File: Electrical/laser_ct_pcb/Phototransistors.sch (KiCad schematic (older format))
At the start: 48 parts, among them Q1 Q_Photo_NPN, Q10 Q_Photo_NPN, Q11 Q_Photo_NPN, Q12 Q_Photo_NPN, Q13 Q_Photo_NPN, Q14 Q_Photo_NPN, Q15 Q_Photo_NPN, Q16 Q_Photo_NPN, Q17 Q_Photo_NPN, Q18 Q_Photo_NPN, Q19 Q_Photo_NPN, Q2 Q_Photo_NPN, Q20 Q_Photo_NPN, Q21 Q_Photo_NPN, Q22 Q_Photo_NPN, Q23 Q_Photo_NPN, Q24 Q_Photo_NPN, Q3 Q_Photo_NPN, Q4 Q_Photo_NPN, Q5 Q_Photo_NPN, Q6 Q_Photo_NPN, Q7 Q_Photo_NPN, Q8 Q_Photo_NPN, Q9 Q_Photo_NPN

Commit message: End of Episode 08.
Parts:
- removed Q1, Q2, Q3, Q4: Q_Photo_NPN, LED_THT:LED_D3.0mm, symbol Device:Q_Photo_NPN
- removed Q10, Q11, Q12, Q13, Q14, Q15, Q16, Q17, Q18, Q19, Q20, Q21, Q22, Q23, Q24, Q5, Q6, Q7, Q8, Q9: Q_Photo_NPN, symbol Device:Q_Photo_NPN
- removed R1, R2, R3, R4: 1 kOhm, Resistor_SMD:R_1206_3216Metric, symbol Device:R_US
- removed R10, R11, R12, R13, R14, R15, R16, R17, R18, R19, R20, R21, R22, R23, R24, R5, R6, R7, R8, R9: 1 kOhm, symbol Device:R_US
- added Q? (x24): Q_Photo_NPN, symbol Device:Q_Photo_NPN
- added R? (x24): 1 kOhm, symbol Device:R_US
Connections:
- net +5V: now also R?.1, R?.1, R?.1, R?.1, R?.1, R?.1, R?.1, R?.1, R?.1, R?.1, R?.1, R?.1, R?.1, R?.1, R?.1, R?.1, R?.1, R?.1, R?.1, R?.1, R?.1, R?.1, R?.1, R?.1
- net GND: now also Q?.2 (E), Q?.2 (E), Q?.2 (E), Q?.2 (E), Q?.2 (E), Q?.2 (E), Q?.2 (E), Q?.2 (E), Q?.2 (E), Q?.2 (E), Q?.2 (E), Q?.2 (E), Q?.2 (E), Q?.2 (E), Q?.2 (E), Q?.2 (E), Q?.2 (E), Q?.2 (E), Q?.2 (E), Q?.2 (E), Q?.2 (E), Q?.2 (E), Q?.2 (E), Q?.2 (E)
- new net PT1: Q?.1 (C), R?.2
- new net PT10: Q?.1 (C), R?.2
- new net PT11: Q?.1 (C), R?.2
- new net PT12: Q?.1 (C), R?.2
- new net PT13: Q?.1 (C), R?.2
- new net PT14: Q?.1 (C), R?.2
- new net PT15: Q?.1 (C), R?.2
- new net PT16: Q?.1 (C), R?.2
- new net PT17: Q?.1 (C), R?.2
- new net PT18: Q?.1 (C), R?.2
- new net PT19: Q?.1 (C), R?.2
- new net PT2: Q?.1 (C), R?.2
- new net PT20: Q?.1 (C), R?.2
- new net PT21: Q?.1 (C), R?.2
- new net PT22: Q?.1 (C), R?.2
- new net PT23: Q?.1 (C), R?.2
- new net PT24: Q?.1 (C), R?.2
- new net PT3: Q?.1 (C), R?.2
- new net PT4: Q?.1 (C), R?.2
- new net PT5: Q?.1 (C), R?.2
- new net PT6: Q?.1 (C), R?.2
- new net PT7: Q?.1 (C), R?.2
- new net PT8: Q?.1 (C), R?.2
- new net PT9: Q?.1 (C), R?.2

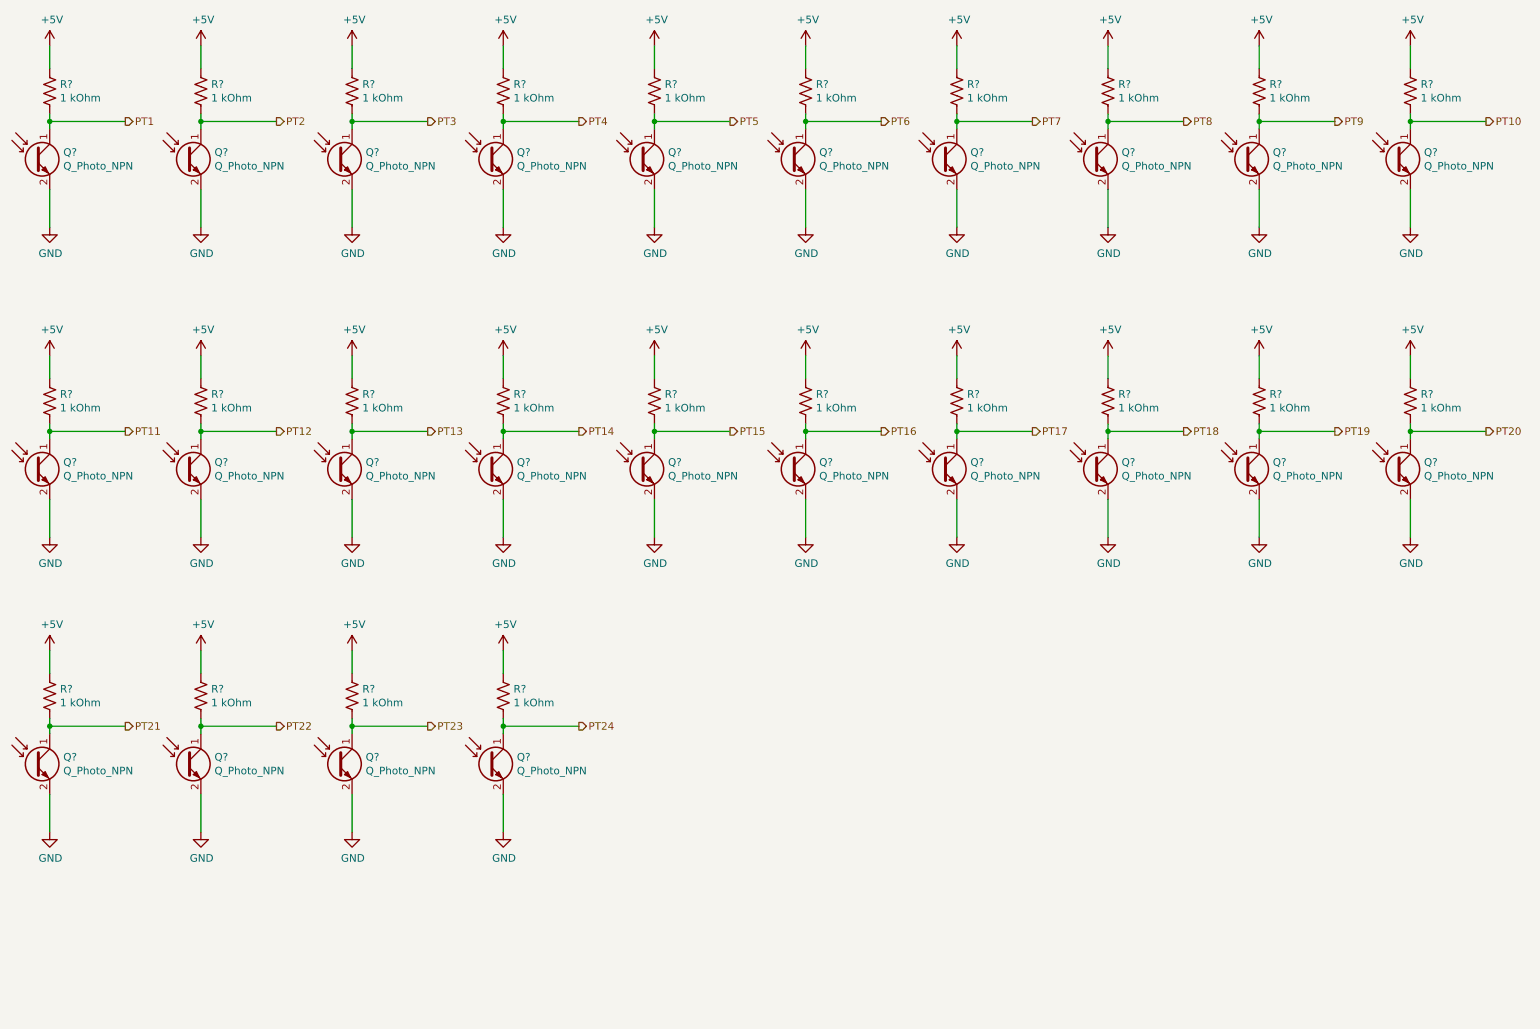
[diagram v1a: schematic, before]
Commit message: Fixed through hole size on ICSP board.
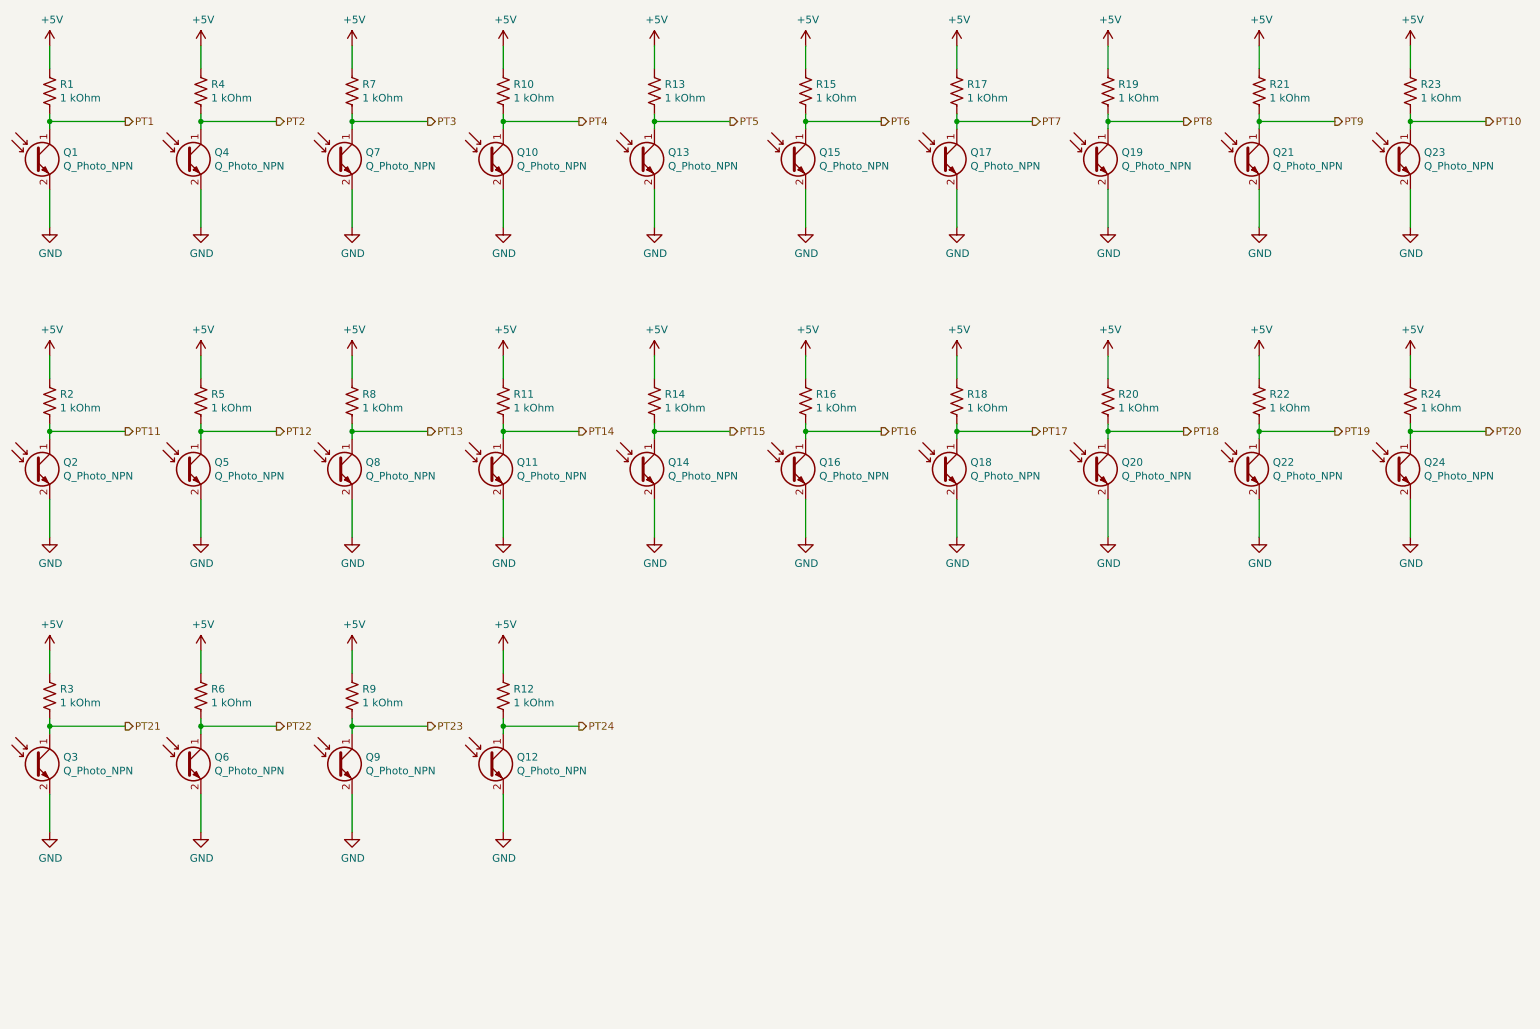
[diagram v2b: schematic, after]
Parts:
- Q1, Q10, Q11, Q12, Q13, Q14, Q15, Q16, Q17, Q18, Q19, Q2, Q20, Q21, Q22, Q23, Q24, Q3, Q4, Q5, Q6, Q7, Q8, Q9: renamed from Q?; footprint (none) -> laser_ct:LTR_301
- R1, R10, R11, R12, R13, R14, R15, R16, R17, R18, R19, R2, R20, R21, R22, R23, R24, R3, R4, R5, R6, R7, R8, R9: renamed from R?; footprint (none) -> Resistor_THT:R_Axial_DIN0204_L3.6mm_D1.6mm_P7.62mm_Horizontal

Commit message: End of episode 09.
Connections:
- net PT10: now also Q10.1 (C), R10.2; no longer Q23.1 (C), R23.2
- net PT11: now also Q11.1 (C), R11.2; no longer Q2.1 (C), R2.2
- net PT12: now also Q12.1 (C), R12.2; no longer Q5.1 (C), R5.2
- net PT13: now also Q13.1 (C), R13.2; no longer Q8.1 (C), R8.2
- net PT14: now also Q14.1 (C), R14.2; no longer Q11.1 (C), R11.2
- net PT15: now also Q15.1 (C), R15.2; no longer Q14.1 (C), R14.2
- net PT17: now also Q17.1 (C), R17.2; no longer Q18.1 (C), R18.2
- net PT18: now also Q18.1 (C), R18.2; no longer Q20.1 (C), R20.2
- net PT19: now also Q19.1 (C), R19.2; no longer Q22.1 (C), R22.2
- net PT2: now also Q2.1 (C), R2.2; no longer Q4.1 (C), R4.2
- net PT20: now also Q20.1 (C), R20.2; no longer Q24.1 (C), R24.2
- net PT21: now also Q21.1 (C), R21.2; no longer Q3.1 (C), R3.2
- net PT22: now also Q22.1 (C), R22.2; no longer Q6.1 (C), R6.2
- net PT23: now also Q23.1 (C), R23.2; no longer Q9.1 (C), R9.2
- net PT24: now also Q24.1 (C), R24.2; no longer Q12.1 (C), R12.2
- net PT3: now also Q3.1 (C), R3.2; no longer Q7.1 (C), R7.2
- net PT4: now also Q4.1 (C), R4.2; no longer Q10.1 (C), R10.2
- net PT5: now also Q5.1 (C), R5.2; no longer Q13.1 (C), R13.2
- net PT6: now also Q6.1 (C), R6.2; no longer Q15.1 (C), R15.2
- net PT7: now also Q7.1 (C), R7.2; no longer Q17.1 (C), R17.2
- net PT8: now also Q8.1 (C), R8.2; no longer Q19.1 (C), R19.2
- net PT9: now also Q9.1 (C), R9.2; no longer Q21.1 (C), R21.2
